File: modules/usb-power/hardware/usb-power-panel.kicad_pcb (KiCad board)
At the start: 2 copper layers, 9.8 x 128.5 mm, 6 parts

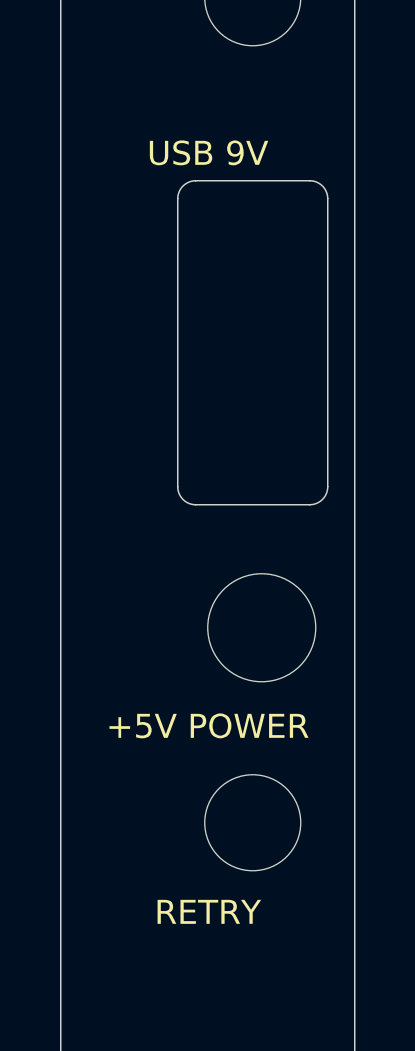
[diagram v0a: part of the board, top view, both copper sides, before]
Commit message: Chanege front panel to give space for L1 Remove tests & release files.
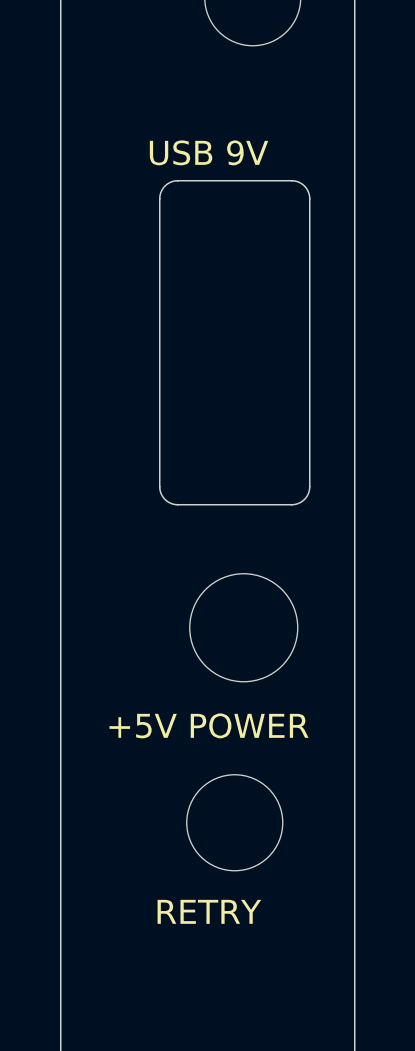
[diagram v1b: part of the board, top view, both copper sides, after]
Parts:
- moved ? 0.60 mm to (55.8, 79.5)
- moved ? 0.60 mm to (56.1, 73.0)
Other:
- outline, holes or cut-outs redrawn
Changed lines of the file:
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@@
 	(footprint ""
 		(layer "F.Cu")
-		(at 56.4 79.5)
+		(at 55.8 79.5)
 		(property "Reference" ""
 			(at 0 0 0)
@@
 	(footprint ""
 		(layer "F.Cu")
-		(at 56.7 73)
+		(at 56.1 73)
 		(property "Reference" ""
 			(at 0 0 0)
@@
 	)
 	(gr_arc
-		(start 53.9 58.7)
-		(mid 54.075735 58.275735)
-		(end 54.5 58.1)
-		(stroke
-			(width 0.05)
-			(type default)
-		)
-		(layer "Edge.Cuts")
-	)
-	(gr_line
-		(start 53.9 68.3)
-		(end 53.9 58.7)
-		(stroke
-			(width 0.05)
-			(type default)
-		)
-		(layer "Edge.Cuts")
-	)
-	(gr_line
-		(start 54.5 58.1)
-		(end 58.3 58.1)
+		(start 53.3 58.7)
+		(mid 53.475735 58.275735)
+		(end 53.9 58.1)
+		(stroke
+			(width 0.05)
+			(type default)
+		)
+		(layer "Edge.Cuts")
+	)
+	(gr_line
+		(start 53.3 68.3)
+		(end 53.3 58.7)
+		(stroke
+			(width 0.05)
+			(type default)
+		)
+		(layer "Edge.Cuts")
+	)
+	(gr_line
+		(start 53.9 58.1)
+		(end 57.699999 58.1)
 		(stroke
 			(width 0.05)
@@
 	)
 	(gr_arc
-		(start 54.5 68.9)
-		(mid 54.075735 68.724264)
-		(end 53.9 68.3)
+		(start 53.9 68.9)
+		(mid 53.475735 68.724264)
+		(end 53.3 68.3)
 		(stroke
 			(width 0.05)
@@
 	)
 	(gr_arc
-		(start 58.3 58.1)
-		(mid 58.724264 58.275735)
-		(end 58.9 58.7)
-		(stroke
-			(width 0.05)
-			(type default)
-		)
-		(layer "Edge.Cuts")
-	)
-	(gr_line
-		(start 58.3 68.9)
-		(end 54.5 68.9)
-		(stroke
-			(width 0.05)
-			(type default)
-		)
-		(layer "Edge.Cuts")
-	)
-	(gr_line
-		(start 58.9 58.7)
-		(end 58.9 68.3)
+		(start 57.699999 58.1)
+		(mid 58.124264 58.275735)
+		(end 58.3 58.7)
+		(stroke
+			(width 0.05)
+			(type default)
+		)
+		(layer "Edge.Cuts")
+	)
+	(gr_line
+		(start 57.699999 68.9)
+		(end 53.9 68.9)
+		(stroke
+			(width 0.05)
+			(type default)
+		)
+		(layer "Edge.Cuts")
+	)
+	(gr_line
+		(start 58.3 58.7)
+		(end 58.3 68.3)
 		(stroke
 			(width 0.05)
@@
 	)
 	(gr_arc
-		(start 58.9 68.3)
-		(mid 58.724264 68.724264)
-		(end 58.3 68.9)
-		(stroke
-			(width 0.05)
+		(start 58.3 68.3)
+		(mid 58.124264 68.724264)
+		(end 57.699999 68.9)
+		(stroke
+			(width 0.05)
